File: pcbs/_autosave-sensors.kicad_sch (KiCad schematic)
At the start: 68 parts

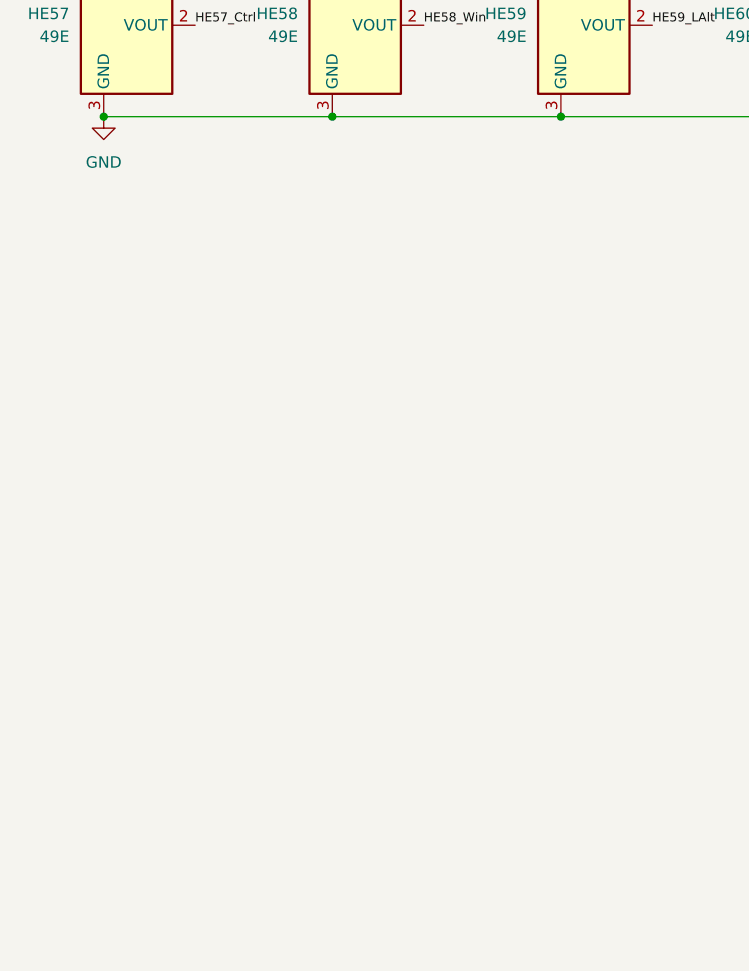
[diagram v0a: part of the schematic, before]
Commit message: usb enumerated, cdc working to print adc voltages
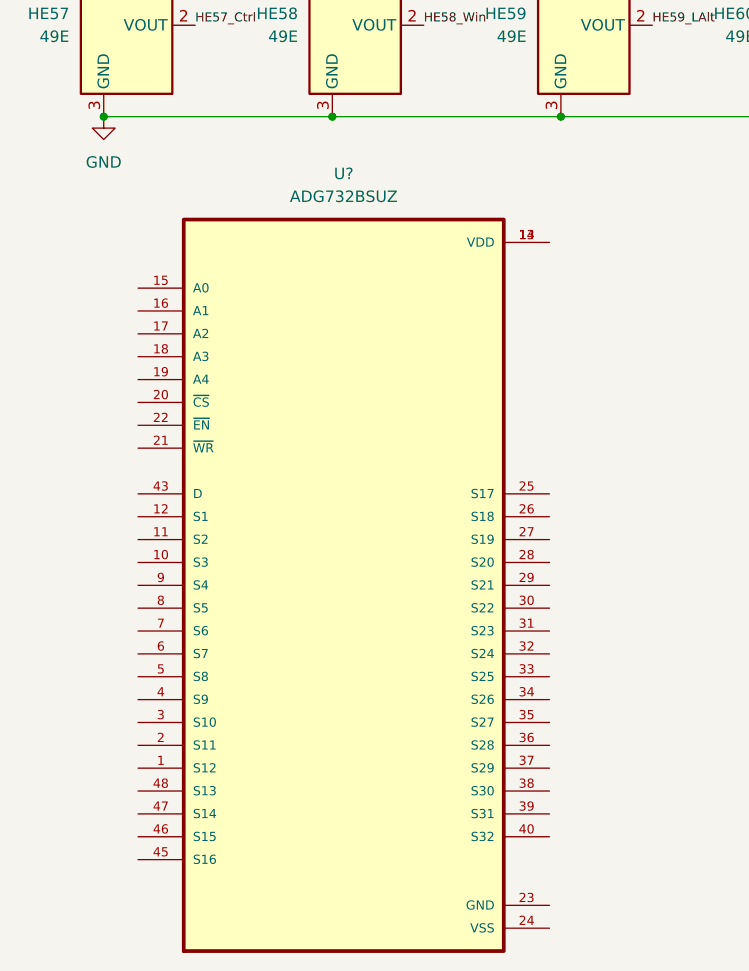
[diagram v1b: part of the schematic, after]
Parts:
- added U?: ADG732BSUZ, ADG732BSUZ:QFP50P900X900X120-49N, symbol ADG732BSUZ:ADG732BSUZ
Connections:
- new net: U?.13 (VDD), U?.14 (VDD)
